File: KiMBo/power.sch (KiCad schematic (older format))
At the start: 27 parts, among them Q1 Q_PNP_BCE, Q2 Q_PNP_BCE, SW1 RESET, SW2 Power, U2 OSD3358, U3 74LVC1G06

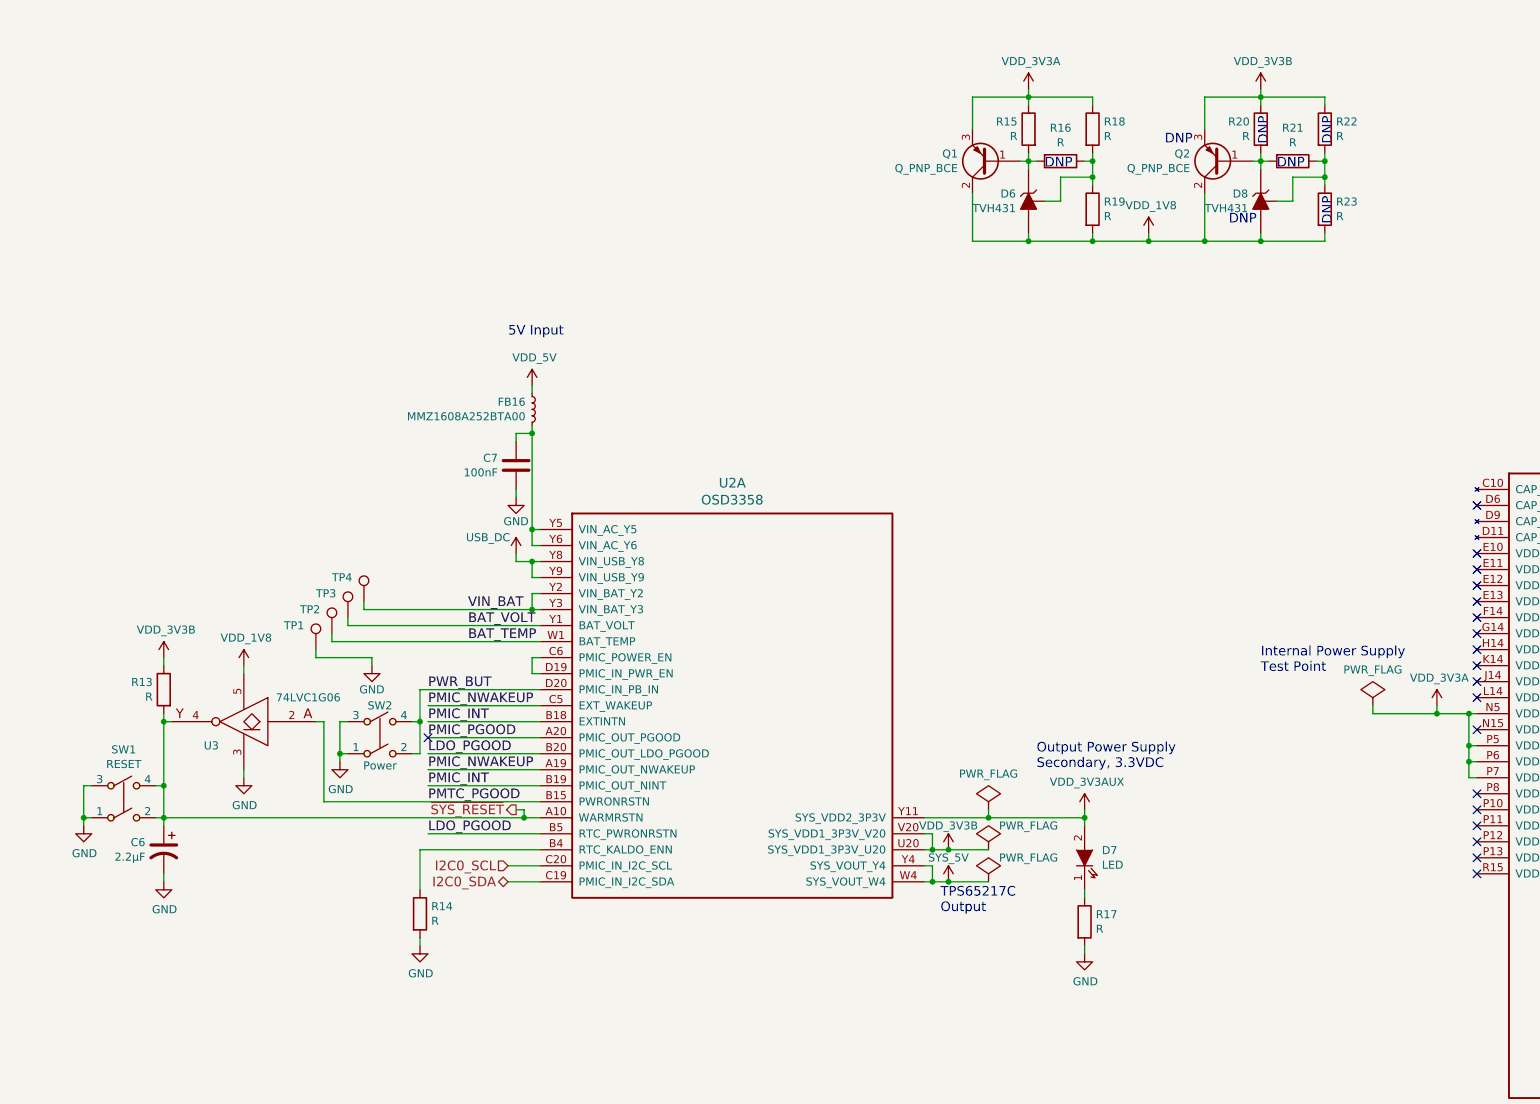
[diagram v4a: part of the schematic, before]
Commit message: Entry of additional component values
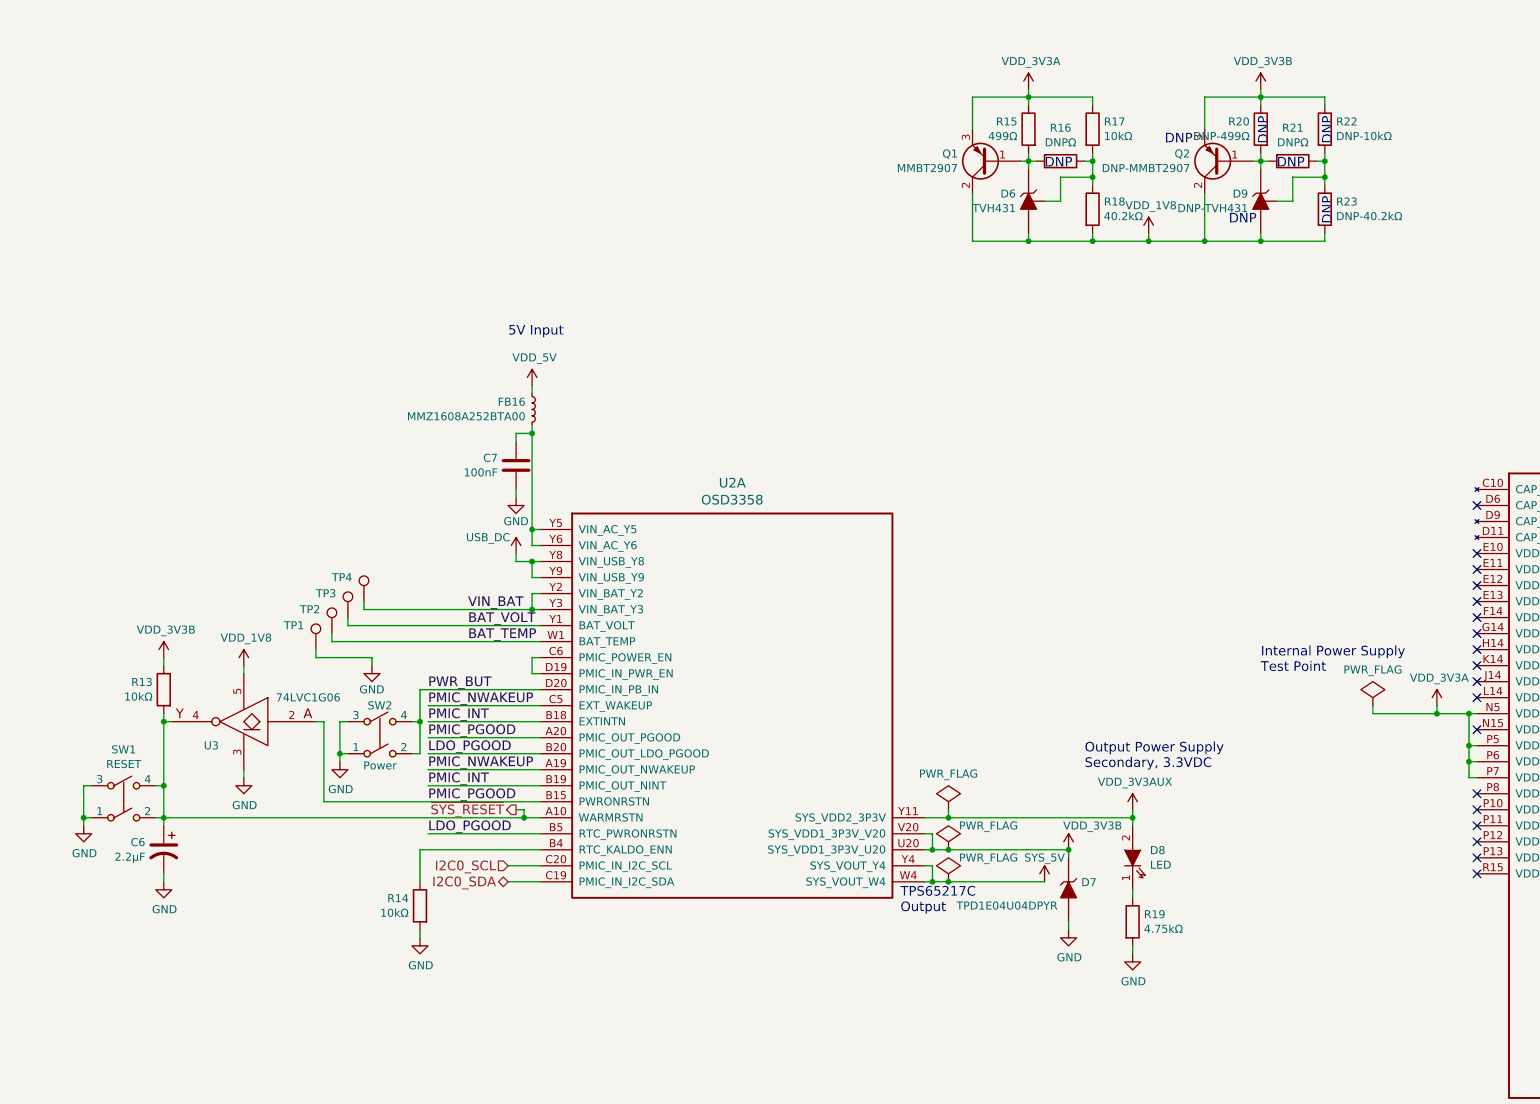
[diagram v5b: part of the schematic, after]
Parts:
- added D7: TPD1E04U04DPYR, symbol ZENER
- D9: renamed from D8; value TVH431 -> DNP-TVH431
- Q1: value Q_PNP_BCE -> MMBT2907
- Q2: value Q_PNP_BCE -> DNP-MMBT2907
- R13, R14: value R -> 10kΩ
- R15: value R -> 499Ω
- R16, R21: value R -> DNPΩ
- R17: renamed from R18; value R -> 10kΩ
- R18: renamed from R19; value R -> 40.2kΩ
- R19: renamed from R17; value R -> 4.75kΩ
- R20: value R -> DNP-499Ω
- R22: value R -> DNP-10kΩ
- R23: value R -> DNP-40.2kΩ
- renumbered D7 to D8
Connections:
- net PMTC_PGOOD is gone; now on net PMIC_PGOOD: U2.B15 (PWRONRSTN), U3.2
- net GND: now also D7.2 (A)
- net VDD_3V3B: now also D7.1 (K)
- no-connect marks 60 -> 59
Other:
- moved on the sheet: D8, R14, R19

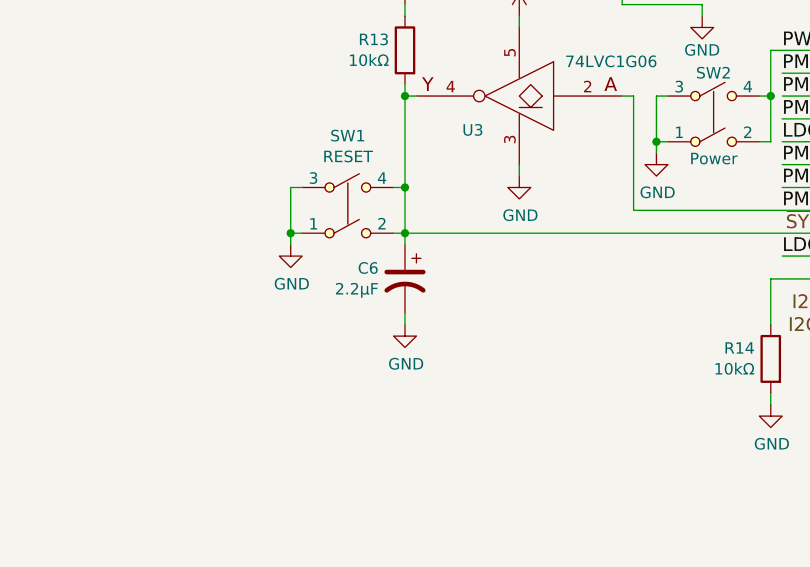
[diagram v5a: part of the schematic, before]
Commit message: Replace most electrolytic cap symbols symbols with the standard, non-polarized (ceramic) cap symbol
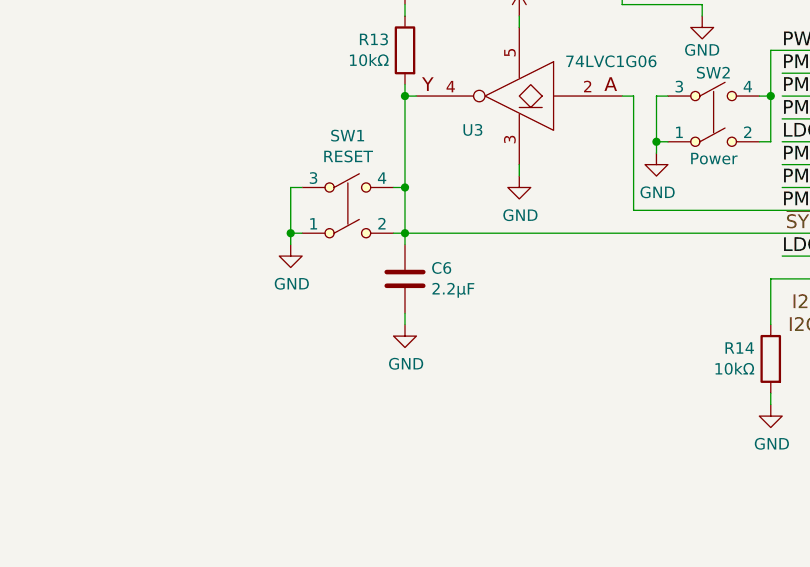
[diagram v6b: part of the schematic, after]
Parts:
- removed C6: 2.2μF, symbol CP1
- added C6: 2.2μF, symbol C
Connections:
- net GND: now also C6.2
- net ~SYS_RESET: now also C6.1
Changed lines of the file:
@@
-$EndComp
-$Comp
-L CP1 C6
-U 1 1 5833746E
-P 4600 6750
-F 0 "C6" H 4715 6796 50  0000 L CNN
-F 1 "2.2μF" H 4715 6705 50  0000 L CNN
-F 2 "" H 4600 6750 50  0001 C CNN
-F 3 "" H 4600 6750 50  0000 C CNN
-	1    4600 6750
-	-1   0    0    -1
 $EndComp
 $Comp
@@
 F 0 "D7" V 10204 7079 50  0000 L CNN
 F 1 "TPD1E04U04DPYR" V 10350 6300 50  0000 L CNN
-F 2 "" H 10250 7000 50  0000 C CNN
+F 2 "" H 10250 7000 50  0001 C CNN
 F 3 "" H 10250 7000 50  0000 C CNN
 	1    10250 7000
@@
 	9350 6950 10100 6950
 Connection ~ 9500 6950
+$Comp
+L C C6
+U 1 1 58E8BEB6
+P 4600 6750
+F 0 "C6" H 4715 6796 50  0000 L CNN
+F 1 "2.2μF" H 4715 6705 50  0000 L CNN
+F 2 "" H 4638 6600 50  0000 C CNN
+F 3 "" H 4600 6750 50  0000 C CNN
+	1    4600 6750
+	1    0    0    -1
+$EndComp
 $EndSCHEMATC

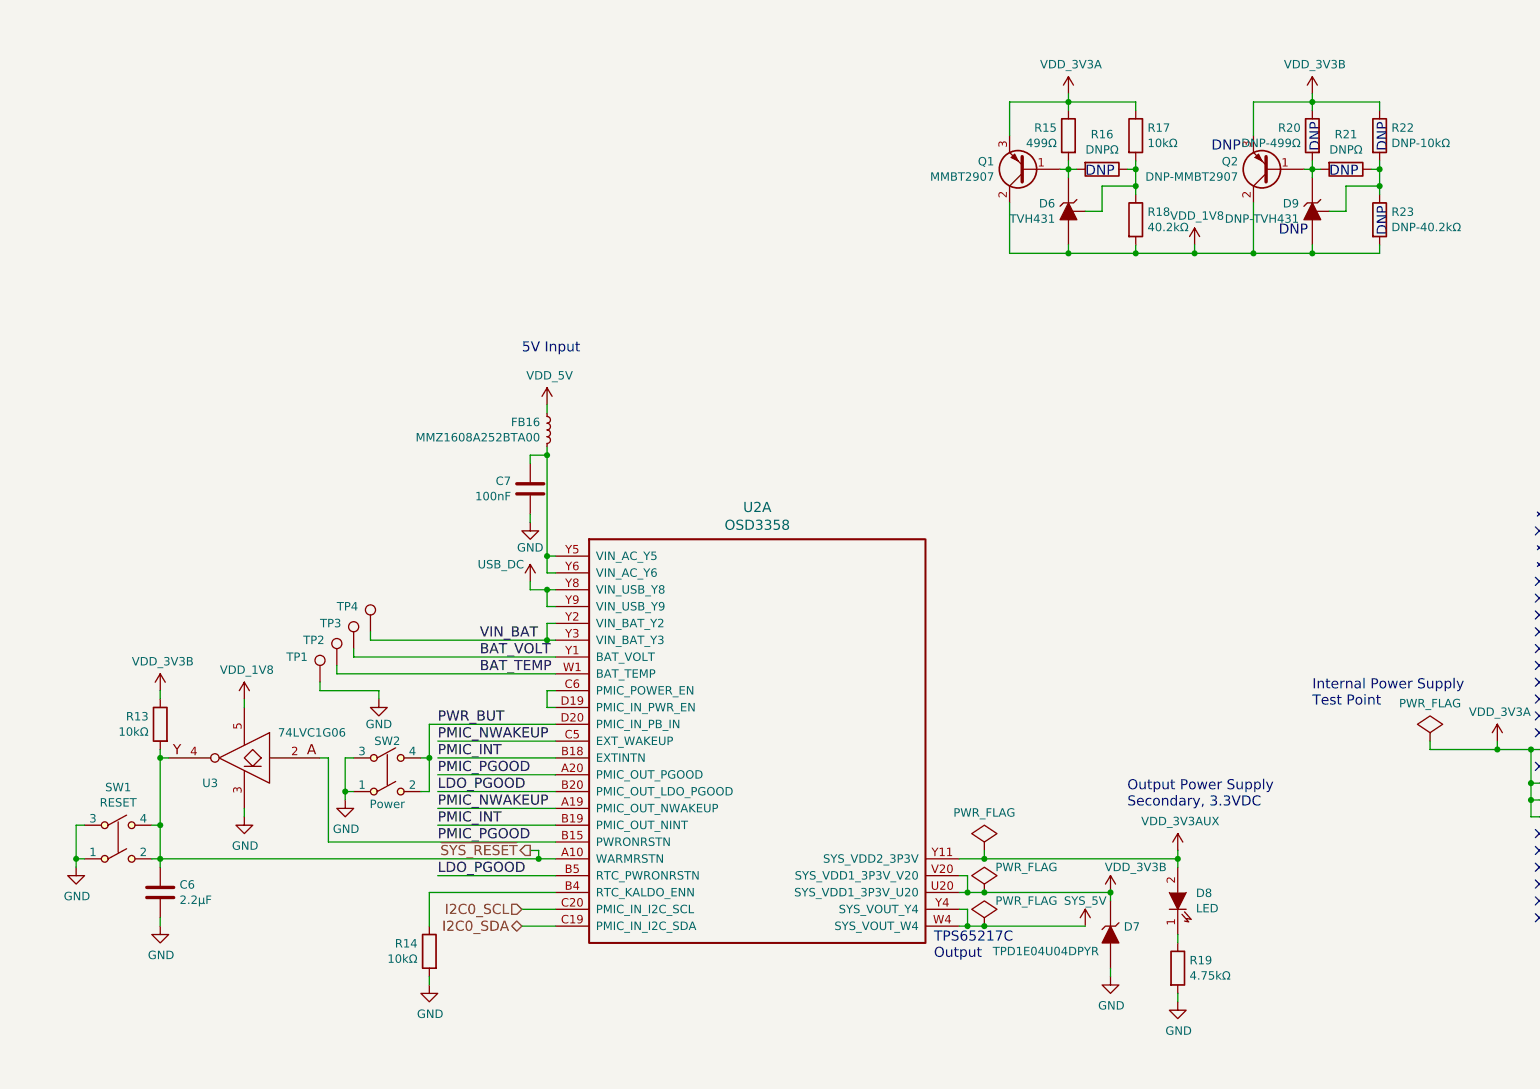
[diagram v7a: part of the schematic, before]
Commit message: Add equivalent annotations document, associate more footprints
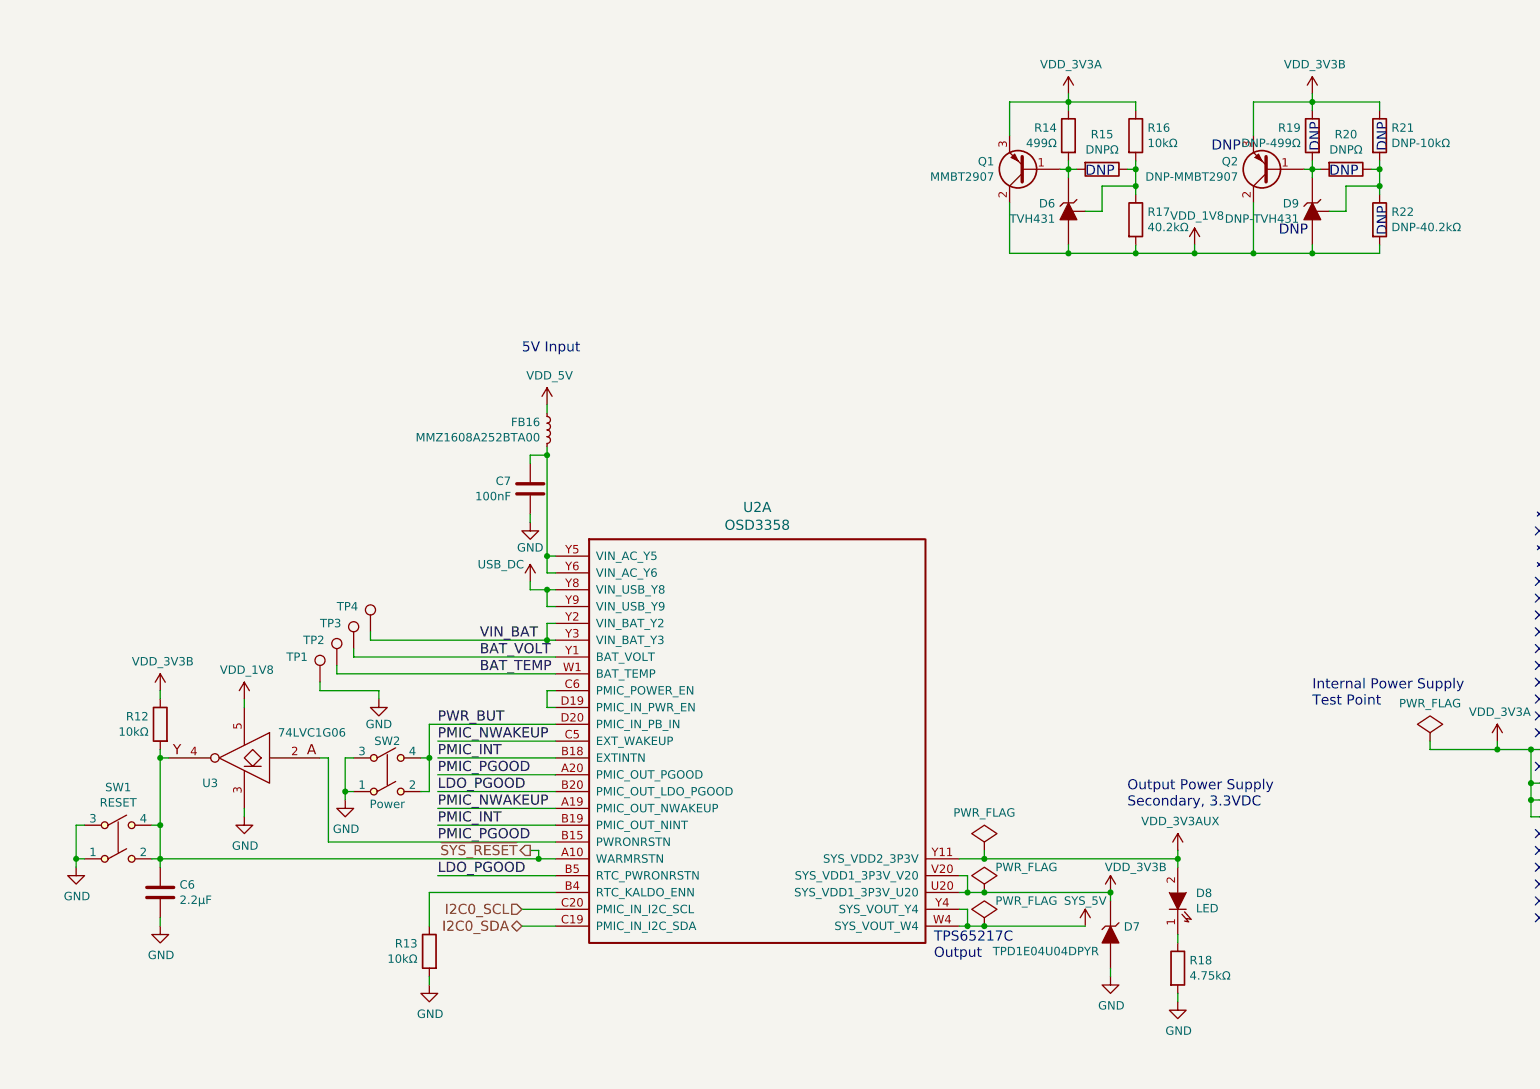
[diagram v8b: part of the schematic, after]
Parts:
- C6: footprint (none) -> Capacitors_SMD:C_0603
- C7: footprint (none) -> Capacitors_SMD:C_0402
- R12: renamed from R13; footprint (none) -> Resistors_SMD:R_0402
- R13: renamed from R14; footprint (none) -> Resistors_SMD:R_0402
- R14: renamed from R15; footprint (none) -> Resistors_SMD:R_0402
- R15: renamed from R16; footprint (none) -> Resistors_SMD:R_0402
- R16: renamed from R17; footprint (none) -> Resistors_SMD:R_0402
- R17: renamed from R18; footprint (none) -> Resistors_SMD:R_0402
- R18: renamed from R19; footprint (none) -> Resistors_SMD:R_0402
- R19: renamed from R20; footprint (none) -> Resistors_SMD:R_0402
- R20: renamed from R21; footprint (none) -> Resistors_SMD:R_0402
- R21: renamed from R22; footprint (none) -> Resistors_SMD:R_0402
- R22: renamed from R23; footprint (none) -> Resistors_SMD:R_0402
